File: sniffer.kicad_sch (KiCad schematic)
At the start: 44 parts, among them J1 TRACK, J2 TRACK, Q1 BC857B, Q2 BC857B, Q3 BC857B, Q4 BC857B, U1 LM393, U2 TL431A, U3 SLHT50H, U4 HCPL2630SDM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

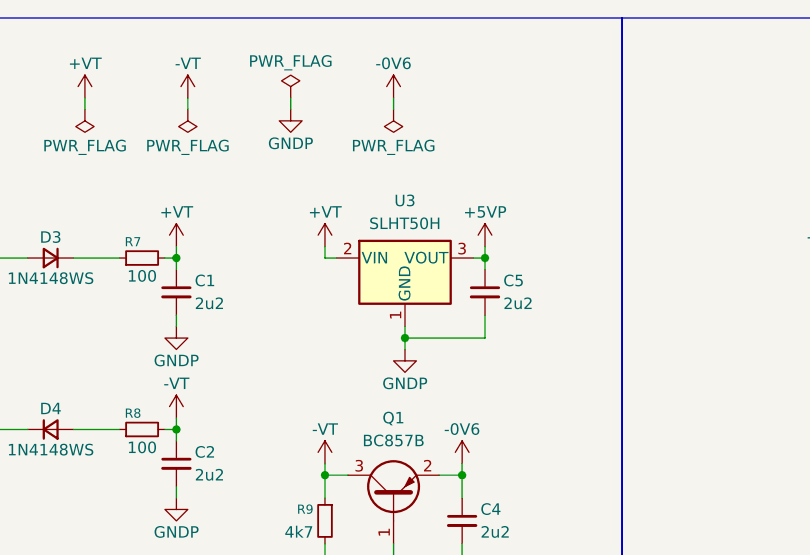
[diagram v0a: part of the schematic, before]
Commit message: fix: U3 regulator pins flipped (#1)
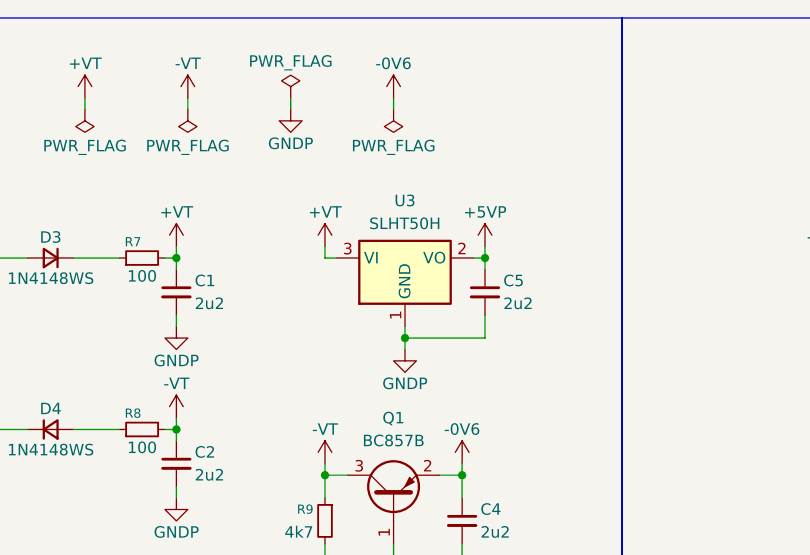
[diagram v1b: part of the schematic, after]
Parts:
- removed U3: SLHT50H, Package_TO_SOT_SMD:SOT-23_Handsoldering, symbol Regulator_Linear:AP2204RA-3.3
- added U3: SLHT50H, Package_TO_SOT_SMD:SOT-23_Handsoldering, symbol Regulator_Linear:LD1117S12TR_SOT223
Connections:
- net +5VP: now also U3.2 (VO)
- net +VT: now also U3.3 (VI)
- net GNDP: now also U3.1 (GND)
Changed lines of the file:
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@@
 	(title_block
 		(title "Sniffer")
-		(date "2026-05-29")
-		(rev "0.1.0")
+		(date "2026-06-23")
+		(rev "0.1.1")
 	)
 	(rectangle
@@
 	)
 	(symbol
+		(lib_id "Regulator_Linear:LD1117S12TR_SOT223")
+		(at 152.4 40.64 0)
+		(unit 1)
+		(body_style 1)
+		(exclude_from_sim no)
+		(in_bom yes)
+		(on_board yes)
+		(in_pos_files yes)
+		(dnp no)
+		(fields_autoplaced yes)
+		(property "Reference" "U3"
+			(at 152.4 34.29 0)
+			(show_name no)
+			(do_not_autoplace no)
+			(effects
+				(font
+					(size 1.27 1.27)
+				)
+			)
+		)
+		(property "Value" "SLHT50H"
+			(at 152.4 36.83 0)
+			(show_name no)
+			(do_not_autoplace no)
+			(effects
+				(font
+					(size 1.27 1.27)
+				)
+			)
+		)
+		(property "Footprint" "Package_TO_SOT_SMD:SOT-23_Handsoldering"
+			(at 152.4 35.56 0)
+			(hide yes)
+			(show_name no)
+			(do_not_autoplace no)
+			(effects
+				(font
+					(size 1.27 1.27)
+				)
+			)
+		)
+		(property "Datasheet" "http://www.st.com/st-web-ui/static/active/en/resource/technical/document/datasheet/CD00000544.pdf"
+			(at 154.94 46.99 0)
+			(hide yes)
+			(show_name no)
+			(do_not_autoplace no)
+			(effects
+				(font
+					(size 1.27 1.27)
+				)
+			)
+		)
+		(property "Description" "800mA Fixed Low Drop Positive Voltage Regulator, Fixed Output 1.2V, SOT-223"
+			(at 152.4 40.64 0)
+			(hide yes)
+			(show_name no)
+			(do_not_autoplace no)
+			(effects
+				(font
+					(size 1.27 1.27)
+				)
+			)
+		)
+		(pin "3"
+		)
+		(pin "1"
+		)
+		(pin "2"
+		)
+		(instances
+			(project "sniffer"
+				(path "/0416b2ae-ab0c-4f9b-9c89-23c1433aa799"
+					(reference "U3")
+					(unit 1)
+				)
+			)
+		)
+	)
+	(symbol
 		(lib_id "Device:R_Small")
 		(at 54.61 49.53 90)
@@
 					(unit 1)
 				)
-			)
-		)
-	)
-	(symbol
-		(lib_id "Regulator_Linear:AP2204RA-3.3")
-		(at 152.4 40.64 0)
-		(unit 1)
-		(body_style 1)
-		(exclude_from_sim no)
-		(in_bom yes)
-		(on_board yes)
-		(in_pos_files yes)
-		(dnp no)
-		(fields_autoplaced yes)
-		(property "Reference" "U3"
-			(at 152.4 34.29 0)
-			(show_name no)
-			(do_not_autoplace no)
-			(effects
-				(font
-					(size 1.27 1.27)
-				)
-			)
-		)
-		(property "Value" "SLHT50H"
-			(at 152.4 36.83 0)
-			(show_name no)
-			(do_not_autoplace no)
-			(effects
-				(font
-					(size 1.27 1.27)
-				)
-			)
-		)
-		(property "Footprint" "Package_TO_SOT_SMD:SOT-23_Handsoldering"
-			(at 152.4 34.925 0)
-			(hide yes)
-			(show_name no)
-			(do_not_autoplace no)
-			(effects
-				(font
-					(size 1.27 1.27)
-				)
-			)
-		)
-		(property "Datasheet" "https://www.diodes.com/assets/Datasheets/products_inactive_data/AP2204.pdf"
-			(at 152.4 40.64 0)
-			(hide yes)
-			(show_name no)
-			(do_not_autoplace no)
-			(effects
-				(font
-					(size 1.27 1.27)
-				)
-			)
-		)
-		(property "Description" "150mA low dropout linear regulator, wide input voltage range, 3.3V fixed positive output, SOT-89-3 package"
-			(at 152.4 40.64 0)
-			(hide yes)
-			(show_name no)
-			(do_not_autoplace no)
-			(effects
-				(font
-					(size 1.27 1.27)
-				)
-			)
-		)
-		(pin "3"
-		)
-		(pin "2"
-		)
-		(pin "1"
-		)
-		(instances
-			(project "sniffer"
-				(path "/0416b2ae-ab0c-4f9b-9c89-23c1433aa799"
-					(reference "U3")
-					(unit 1)
-				)

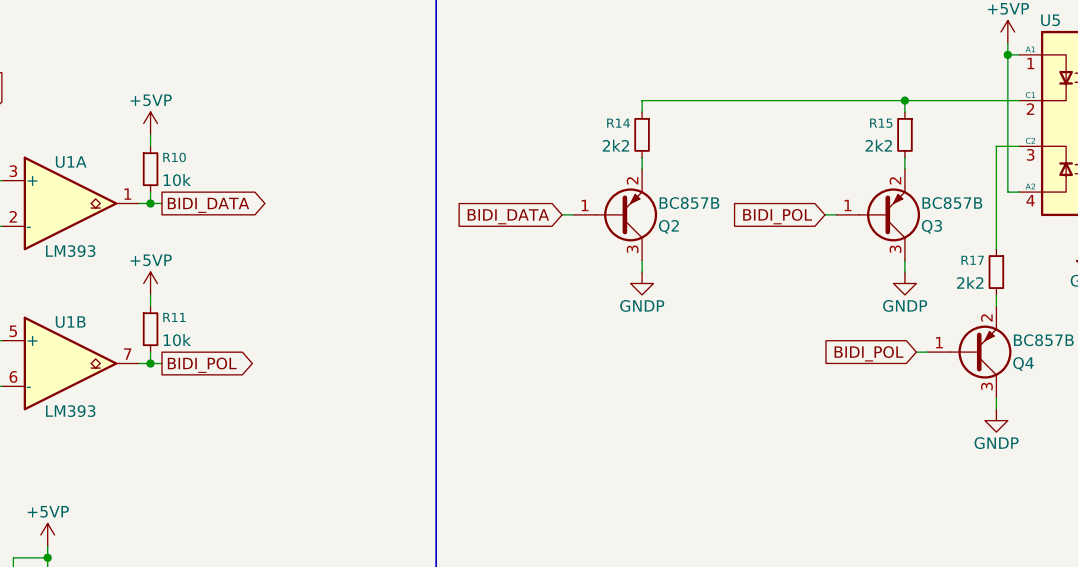
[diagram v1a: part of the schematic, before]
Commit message: chore: suitable names for `BIDI_DATA` and `BIDI_POL`
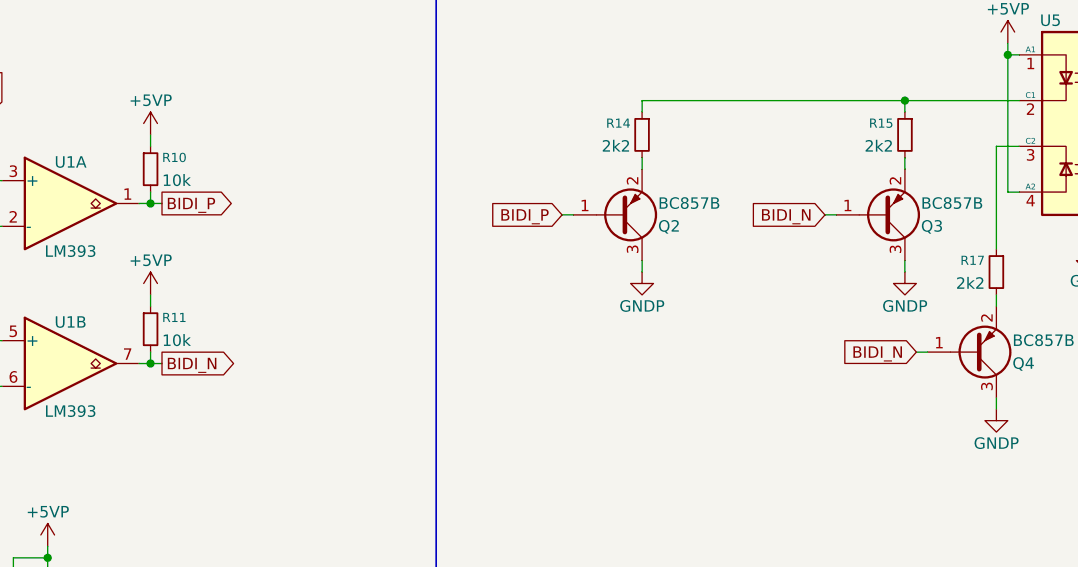
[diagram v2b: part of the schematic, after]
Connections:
- net BIDI_DATA renamed BIDI_P
- net BIDI_POL renamed BIDI_N
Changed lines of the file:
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@@
 		)
 	)
-	(global_label "BIDI_DATA"
+	(global_label "BIDI_P"
 		(shape input)
 		(at 190.5 123.19 180)
@@
 		)
 		(property "Intersheetrefs" "${INTERSHEET_REFS}"
-			(at 178.3828 123.19 0)
+			(at 181.5276 123.19 0)
 			(hide yes)
 			(show_name no)
@@
 		)
 	)
-	(global_label "BIDI_DATA"
+	(global_label "BIDI_P"
 		(shape output)
 		(at 146.05 121.92 0)
@@
 		)
 		(property "Intersheetrefs" "${INTERSHEET_REFS}"
-			(at 158.1672 121.92 0)
-			(hide yes)
-			(show_name no)
-			(do_not_autoplace no)
-			(effects
-				(font
-					(size 1.27 1.27)
-				)
-				(justify left)
-			)
-		)
-	)
-	(global_label "BIDI_POL"
+			(at 155.0224 121.92 0)
+			(hide yes)
+			(show_name no)
+			(do_not_autoplace no)
+			(effects
+				(font
+					(size 1.27 1.27)
+				)
+				(justify left)
+			)
+		)
+	)
+	(global_label "BIDI_N"
 		(shape output)
 		(at 146.05 139.7 0)
@@
 		)
 		(property "Intersheetrefs" "${INTERSHEET_REFS}"
-			(at 157.381 139.7 0)
+			(at 155.0829 139.7 0)
 			(hide yes)
 			(show_name no)
@@
 		)
 	)
-	(global_label "BIDI_POL"
+	(global_label "BIDI_N"
 		(shape input)
 		(at 229.87 138.43 180)
@@
 		)
 		(property "Intersheetrefs" "${INTERSHEET_REFS}"
-			(at 218.539 138.43 0)
+			(at 220.8371 138.43 0)
 			(hide yes)
 			(show_name no)
@@
 		)
 	)
-	(global_label "BIDI_POL"
+	(global_label "BIDI_N"
 		(shape input)
 		(at 219.71 123.19 180)
@@
 		)
 		(property "Intersheetrefs" "${INTERSHEET_REFS}"
-			(at 208.379 123.19 0)
-			(hide yes)
-			(show_name no)
+			(at 210.6771 123.19 0)
+			(hide yes)
+			(show_name no)
